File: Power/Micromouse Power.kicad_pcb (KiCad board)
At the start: 2 copper layers, 44.7 x 28.4 mm, 50 parts, among them J1 Battery, J2 Conn_02x08_Odd_Even, Q1 AO3401A, Q2 AO3401A, SW1 pwr, SW2 pwr, U1 AMS1117-3.3, U2 TP4056, U3 DRV8837, U4 DRV8837

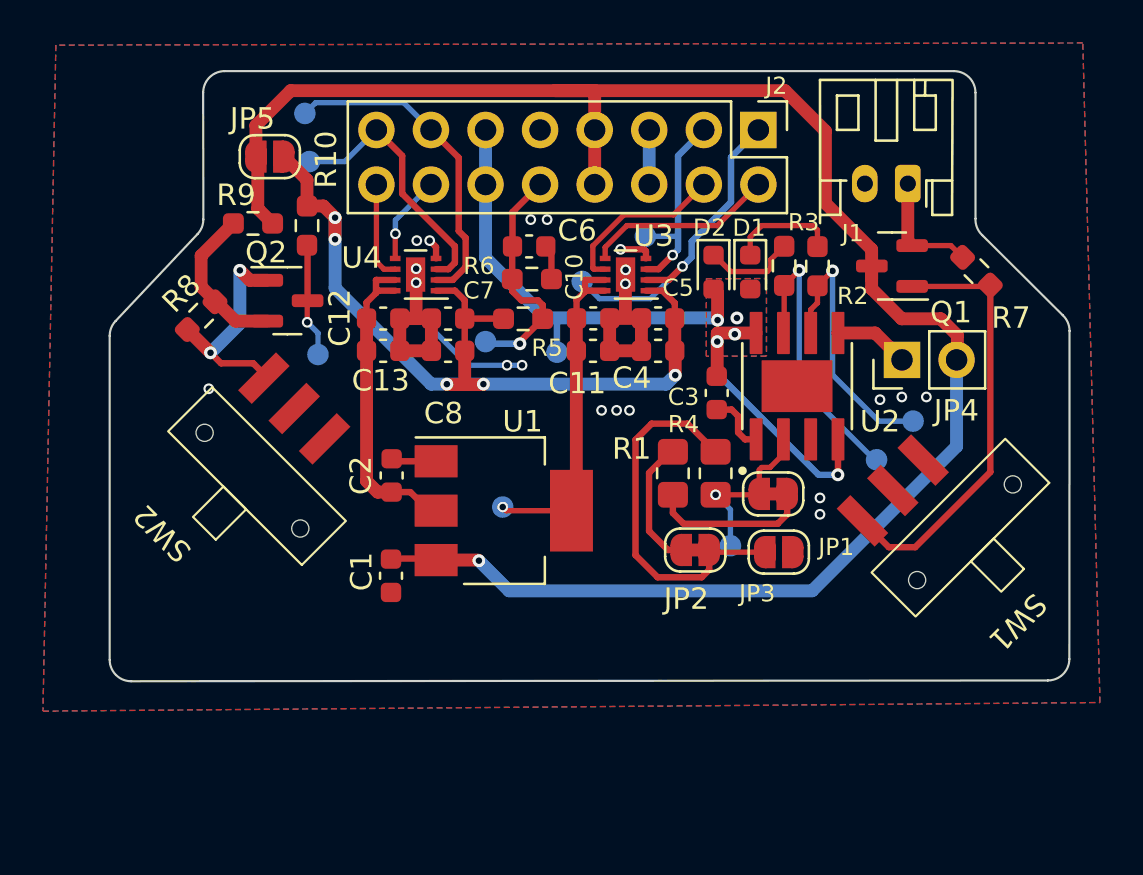
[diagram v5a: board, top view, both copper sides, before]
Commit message: Added switch silkscreen
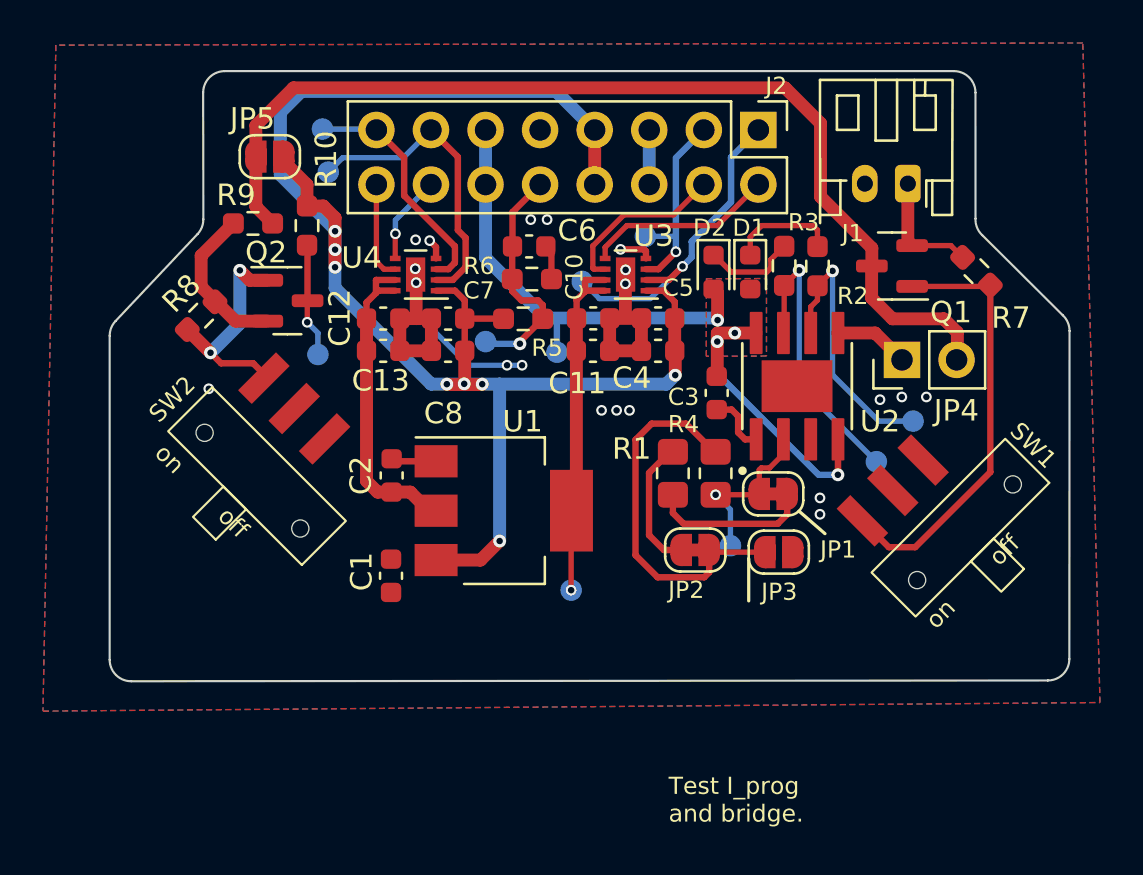
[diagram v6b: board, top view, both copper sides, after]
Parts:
- moved TP9 5.01 mm to (160.9, 129.8)
- moved TP6 2.94 mm to (149.6, 110.3)
- moved TP7 1.63 mm to (149.3, 108.3)
- moved TP2 0.09 mm to (175.1, 123.8)
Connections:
- C1 pad 1: BATT -> BATT_SWITCHED
- J2 pad 7: BATT -> BATT_SWITCHED
- J2 pad 8: BATT -> BATT_SWITCHED
- U1 pad 3: BATT -> BATT_SWITCHED
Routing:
- net BATT: track 87.7 -> 47.3 mm, vias 1 -> 0
- net BATT_SWITCHED: track 40.5 -> 76.5 mm, vias 5 -> 8
- net /Motor1_B: track 12.6 -> 11.2 mm
- net /Motor1_A: track 15.3 -> 14.4 mm
- net +5V: vias 5 -> 4
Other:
- board text added: "- +"
- board text added: "Test I_prog and bridge."
- board text added: "on off"

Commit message: Review and touchups
-added silkscreen art and info
-fixed tp4056 decoupling
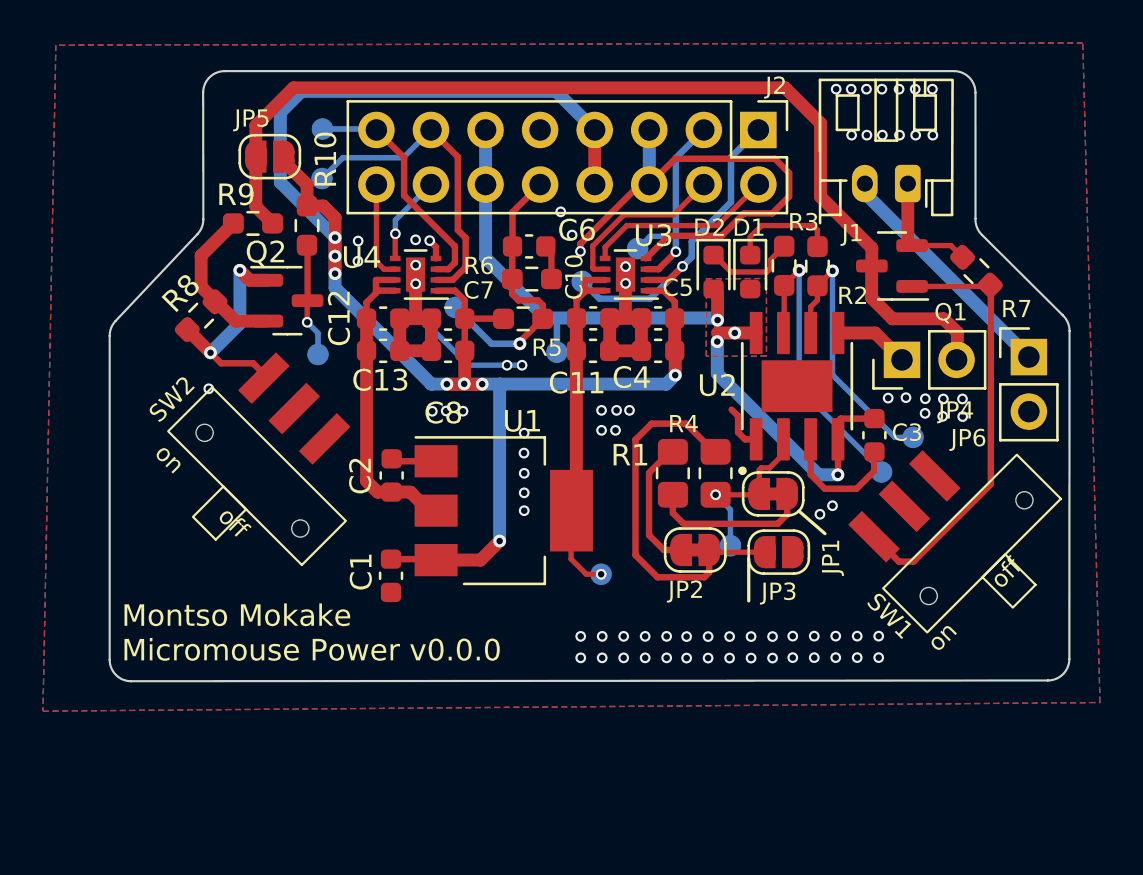
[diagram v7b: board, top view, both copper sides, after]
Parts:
- added G***: LOGO, LOGO, B.Cu at (153.6, 129.2)
- added JP6: I_batt, Connector_PinHeader_2.54mm:PinHeader_1x02_P2.54mm_Vertical, F.Cu at (182.2, 118.9)
- TP4: value M1A -> M2A
- TP5: value M1B -> M2B
- moved C3 7.60 mm to (175.0, 122.6)
- moved TP8 2.13 mm to (155.5, 116.6)
- moved TP9 1.58 mm to (162.3, 129.0), turned to 0 degrees
- moved SW1 0.92 mm to (180.6, 132.9)
- moved TP1 0.76 mm to (176.8, 122.7)
- moved TP5 0.67 mm to (164.0, 113.9)
- moved TP2 0.54 mm to (175.3, 124.3)
- moved TP6 0.42 mm to (149.3, 110.6)
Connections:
- J1 pad 2: GND -> Net-(J1-Pin_2)
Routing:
- net GND: track 34.4 -> 58.6 mm, vias 20 -> 80
- net Net-(J1-Pin_2): track 0.00 -> 11.2 mm
- net BATT_SWITCHED: track 76.5 -> 78.9 mm
- net /BATT_ADC: track 11.2 -> 13.3 mm
- net +5V: track 35.7 -> 37.3 mm
- net Net-(U2-~{CHRG}): track 13.6 -> 14.2 mm
- net /Motor2_B: track 9.34 -> 9.94 mm
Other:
- board text added: "Montso Mokake Micromouse Power v0.0.0"
- board text added: "m2a m2b gnd bat pd7 5v m1a m1b"
- board text added: "pc6 pc7 gnd batt adc 5v pc8 pc9"
- board text removed: "Test I_prog and bridge."

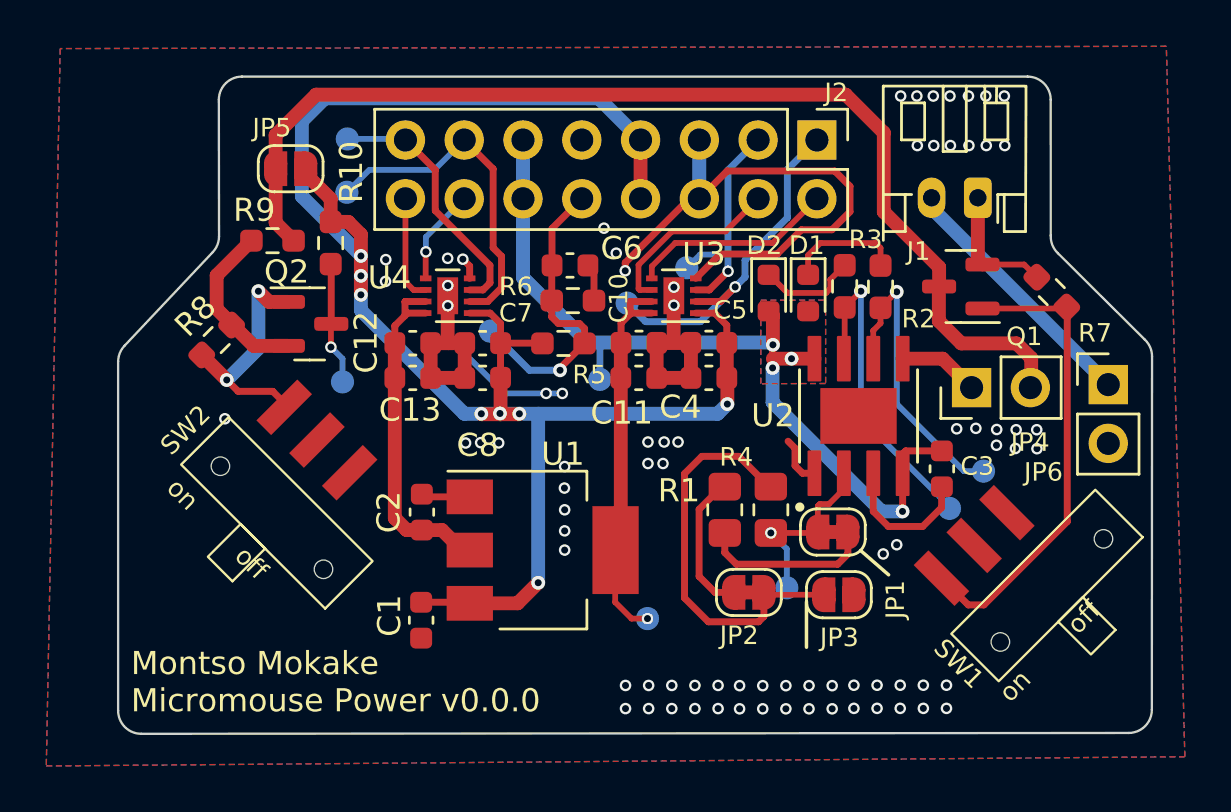
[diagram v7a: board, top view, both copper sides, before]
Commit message: Added VCC divider for driver.
-Jumper to select VCC
-Stitching vias
-Silkscreen
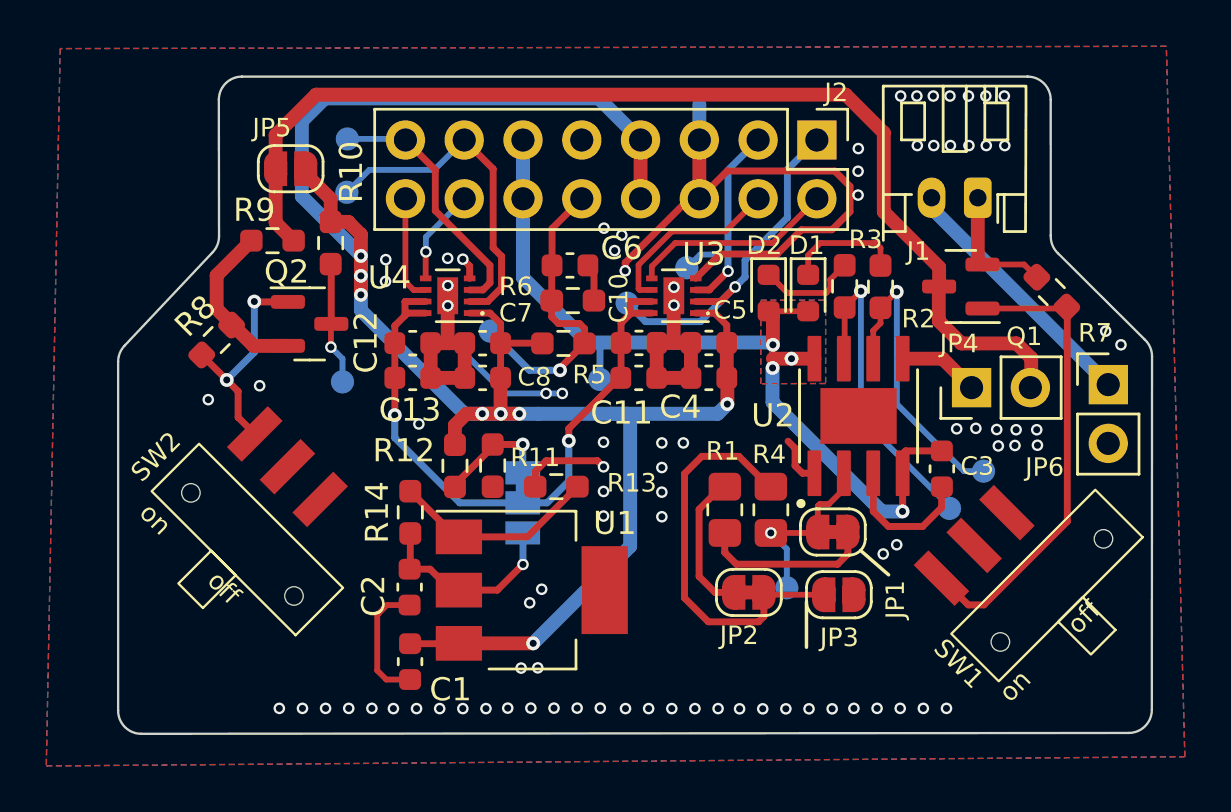
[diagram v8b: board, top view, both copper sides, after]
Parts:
- removed TP9: 3v3, TestPoint:TestPoint_Pad_D1.0mm
- added JP7: VCC, Jumper:SolderJumper-3_P1.3mm_Bridged12_Pad1.0x1.5mm_NumberLabels, B.Cu at (156.9, 124.0)
- added R11: 330R, Resistor_SMD:R_0603_1608Metric_Pad0.98x0.95mm_HandSolder, F.Cu at (155.6, 122.4)
- added R12: 100R, Resistor_SMD:R_0603_1608Metric_Pad0.98x0.95mm_HandSolder, F.Cu at (154.0, 122.4)
- added R13: 0R, Resistor_SMD:R_0603_1608Metric_Pad0.98x0.95mm_HandSolder, F.Cu at (158.3, 123.3)
- added R14: open, Resistor_SMD:R_0603_1608Metric_Pad0.98x0.95mm_HandSolder, F.Cu at (152.0, 124.4)
- moved G*** 6.62 mm to (147.5, 126.6)
- moved C2 3.28 mm to (152.0, 127.7), turned to -90 degrees
- moved C1 1.85 mm to (152.0, 130.9)
- moved U1 1.79 mm to (157.3, 127.8)
- moved SW2 1.72 mm to (139.7, 126.7)
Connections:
- C10 pad 1: +3V3 -> VCC
- C11 pad 1: +3V3 -> VCC
- C12 pad 1: +3V3 -> VCC
- C13 pad 1: +3V3 -> VCC
- U1 pad 1: GND -> Net-(U1-GND)
- U3 pad 7: +3V3 -> VCC
- U3 pad 8: +3V3 -> VCC
- U4 pad 7: +3V3 -> VCC
- U4 pad 8: +3V3 -> VCC
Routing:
- net VCC: track 0.00 -> 27.7 mm, vias 0 -> 2
- net +3V3: track 32.5 -> 8.75 mm
- net Net-(U1-GND): track 0.00 -> 8.94 mm
- net GND: track 58.6 -> 67.4 mm, vias 80 -> 88
- net BATT_SWITCHED: track 78.9 -> 86.0 mm
- net Net-(JP7-A): track 0.00 -> 5.02 mm, vias 0 -> 1
- net +5V: track 37.3 -> 39.0 mm
- net Net-(Q2-G): track 10.5 -> 9.70 mm
